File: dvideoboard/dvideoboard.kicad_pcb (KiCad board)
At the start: 2 copper layers, 64.9 x 48.1 mm, 18 parts, among them IC1 LVC245A, IC2 LVC245A, IC3 LVC245A, IC4 LVC245A, P1 CONN_02X16, P3 JTAG, U1 10M08SC, U2 ADV7513, U3 TC1262-33VDB, U4 TC1262-33VDB, U5 Si501

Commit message: Ongoing development fpga board
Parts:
- removed U4: TC1262-33VDB, TO_SOT_Packages_SMD:SOT-223
- removed U5: Si501, Oscillators:Oscillator_SMD_SeikoEpson_SG8002LB-4pin_5.0x3.2mm_HandSoldering
- added C10: 4.7uF, Capacitors_SMD:C_0805, F.Cu at (183.6, 143.6)
- added C11: 10uF, Capacitors_SMD:C_0805, B.Cu at (177.2, 129.5)
- added C12: 10uF, Capacitors_SMD:C_0805, B.Cu at (180.7, 130.4)
- added C6: 10uF, Capacitors_SMD:C_0805, F.Cu at (164.5, 137.8)
- added C7: 47u, Capacitors_SMD:C_1206, F.Cu at (185.7, 142.7)
- added C8: 4.7u, Capacitors_SMD:C_0805, F.Cu at (173.2, 143.3)
- added C9: 10uF, Capacitors_SMD:C_0805, F.Cu at (175.9, 137.8)
- added D2: LED, LEDs:LED_0805, F.Cu at (130.8, 104.1)
- added F1: 0ZCK0050AF2E, Capacitors_SMD:C_0805, F.Cu at (185.5, 138.2)
- added IC5: EP5388QI, Housings_SSOP:TSSOP-16_4.4x5mm_Pitch0.65mm, F.Cu at (167.4, 143.0)
- added IC6: EP5388QI, Housings_SSOP:TSSOP-16_4.4x5mm_Pitch0.65mm, F.Cu at (178.6, 143.0)
- added L1: 10uH, Capacitors_SMD:C_0805, F.Cu at (163.2, 134.0)
- added L2: 10uH, Capacitors_SMD:C_0805, F.Cu at (166.4, 134.0)
- added L3: 10uH, Capacitors_SMD:C_0805, F.Cu at (168.9, 134.0)
- added L4: 10uH, Capacitors_SMD:C_0805, F.Cu at (171.4, 134.0)
- added L5: 10uH, Capacitors_SMD:C_0805, F.Cu at (174.6, 134.0)
- added L6: 10uH, Capacitors_SMD:C_0805, F.Cu at (177.2, 134.0)
- added L7: 10uH, Capacitors_SMD:C_0805, F.Cu at (179.7, 134.0)
- added P2: POWER, Pin_Headers:Pin_Header_Straight_1x02_Pitch2.54mm, F.Cu at (188.8, 141.7)
- added P4: HDMI-A, footprints:FCI_10029449-11-5B13-5DRLF, F.Cu at (179.3, 119.4)
- added P5: CONN_01X02, Pin_Headers:Pin_Header_Straight_2x01_Pitch2.54mm, F.Cu at (130.8, 100.3)
- added R10: 2K, Resistors_SMD:R_0805, F.Cu at (172.7, 102.9)
- added R11: 2K, Resistors_SMD:R_0805, F.Cu at (170.2, 101.0)
- added R12: 10k, Resistors_SMD:R_0805, F.Cu at (171.4, 125.7)
- added R13: 2K, Resistors_SMD:R_0805, F.Cu at (177.8, 106.0)
- added R14: 2K, Resistors_SMD:R_0805, F.Cu at (180.3, 106.0)
- added R15: 2K, Resistors_SMD:R_0805, F.Cu at (175.3, 104.8)
- added R16: 1K, Resistors_SMD:R_0805, F.Cu at (130.8, 108.6)
- added R2: 10k, Resistors_SMD:R_0805, F.Cu at (124.5, 116.8)
- added R3: 10k, Resistors_SMD:R_0805, F.Cu at (127.0, 116.8)
- added R4: 10k, Resistors_SMD:R_0805, F.Cu at (121.9, 116.8)
- added R5: 10k, Resistors_SMD:R_0805, F.Cu at (129.5, 116.8)
- added R6: 10k, Resistors_SMD:R_0805, F.Cu at (140.3, 99.7)
- added R7: 10k, Resistors_SMD:R_0805, F.Cu at (144.1, 99.7)
- added R8: 10k, Resistors_SMD:R_0805, F.Cu at (148.6, 99.7)
- added R9: 887, Resistors_SMD:R_0805, F.Cu at (168.9, 125.7)
- C1, C2, C3, C4, C5: value 100n -> 10uF; footprint Capacitors_SMD:C_0805_HandSoldering -> Capacitors_SMD:C_0805; moved to B.Cu
- D1: value Led_Small -> LED
- IC1, IC2, IC3, IC4: value LVC245A -> SN74LVC245APWR
- R1: footprint Resistors_SMD:R_0805_HandSoldering -> Resistors_SMD:R_0805
- U1: value 10M08SC -> 10M08SCE144C8G
- U3: value TC1262-33VDB -> TG2016SBN 20.0000M-TCGNNM3; footprint TO_SOT_Packages_SMD:SOT-223 -> Crystals:Crystal_SMD_2016-4pin_2.0x1.6mm
- moved C5 51.9 mm to (174.6, 129.5), turned to 270 degrees
- moved U3 51.7 mm to (123.8, 121.9)
- moved C4 50.3 mm to (171.4, 129.5), turned to 270 degrees
- moved C3 37.6 mm to (168.9, 129.5), turned to 270 degrees
- moved C2 25.0 mm to (166.4, 129.5), turned to 270 degrees
- moved C1 11.9 mm to (163.2, 129.5), turned to 270 degrees
- moved R1 2.69 mm to (133.3, 108.6), turned to 90 degrees
- moved D1 2.01 mm to (133.3, 104.1), turned to 90 degrees
- moved U2 1.27 mm to (168.3, 116.2)
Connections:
- C1 pad 1: Net-(C1-Pad1) -> GND
- C1 pad 2: GND -> /3V3A
- C2 pad 1: Net-(C1-Pad1) -> GND
- C2 pad 2: GND -> /3V3B
- C3 pad 1: Net-(C1-Pad1) -> GND
- C3 pad 2: GND -> /3V3C
- C4 pad 1: Net-(C1-Pad1) -> GND
- C4 pad 2: GND -> /3V3D
- C5 pad 1: Net-(C1-Pad1) -> GND
- C5 pad 2: GND -> /1V8A
- D1 pad 1: GND -> Net-(D1-Pad1)
- IC1 pad 1: Net-(C1-Pad1) -> /3V3A
- IC1 pad 20: Net-(C1-Pad1) -> /3V3A
- IC2 pad 1: Net-(C1-Pad1) -> /3V3A
- IC2 pad 20: Net-(C1-Pad1) -> /3V3A
- IC3 pad 1: Net-(C1-Pad1) -> /3V3A
- IC3 pad 20: Net-(C1-Pad1) -> /3V3A
- IC4 pad 1: Net-(C1-Pad1) -> /3V3A
- IC4 pad 20: Net-(C1-Pad1) -> /3V3A
- P3 pad 4: Net-(C1-Pad1) -> /3V3A
- R1 pad 1: Net-(R1-Pad1) -> GND
- R1 pad 2: Net-(D1-Pad2) -> Net-(D1-Pad1)
- U1 pad 1: Net-(U1-Pad1) -> /3V3B
- U1 pad 103: Net-(U1-Pad103) -> /3V3B
- U1 pad 104: Net-(U1-Pad104) -> GND
- U1 pad 107: Net-(U1-Pad107) -> /3V3C
- U1 pad 108: Net-(U1-Pad108) -> /3V3B
- U1 pad 109: Net-(U1-Pad109) -> /3V3B
- U1 pad 114: Net-(U1-Pad114) -> Net-(R15-Pad2)
- U1 pad 115: Net-(U1-Pad115) -> /3V3B
- U1 pad 116: Net-(U1-Pad116) -> GND
- U1 pad 117: Net-(U1-Pad117) -> /3V3B
- U1 pad 121: Net-(U1-Pad121) -> /3V3B
- U1 pad 122: Net-(U1-Pad122) -> /3V3B
- U1 pad 125: Net-(U1-Pad125) -> GND
- U1 pad 128: Net-(U1-Pad128) -> /3V3B
- U1 pad 129: Net-(U1-Pad129) -> /3V3B
- U1 pad 133: Net-(U1-Pad133) -> GND
- U1 pad 137: Net-(U1-Pad137) -> GND
- U1 pad 139: Net-(U1-Pad139) -> /3V3B
- U1 pad 142: Net-(U1-Pad142) -> GND
- U1 pad 143: Net-(U1-Pad143) -> /3V3C
- U1 pad 144: Net-(U1-Pad144) -> /3V3B
- U1 pad 2: Net-(U1-Pad2) -> /3V3C
- U1 pad 23: Net-(U1-Pad23) -> /3V3B
- U1 pad 3: Net-(U1-Pad3) -> GND
- U1 pad 31: Net-(U1-Pad31) -> /3V3B
- U1 pad 34: Net-(U1-Pad34) -> /3V3C
- U1 pad 35: Net-(U1-Pad35) -> /3V3C
- U1 pad 36: Net-(U1-Pad36) -> /3V3B
- U1 pad 37: Net-(U1-Pad37) -> /3V3B
- U1 pad 4: Net-(U1-Pad4) -> GND
- U1 pad 40: Net-(U1-Pad40) -> /3V3B
- U1 pad 42: Net-(U1-Pad42) -> GND
- U1 pad 49: Net-(U1-Pad49) -> /3V3B
- U1 pad 5: Net-(U1-Pad5) -> /3V3C
- U1 pad 51: Net-(U1-Pad51) -> /3V3B
- U1 pad 53: Net-(U1-Pad53) -> GND
- U1 pad 6: Net-(R1-Pad1) -> Net-(D1-Pad2)
- U1 pad 63: Net-(U1-Pad63) -> GND
- U1 pad 67: Net-(U1-Pad67) -> /3V3B
- U1 pad 68: Net-(U1-Pad68) -> GND
- U1 pad 71: Net-(U1-Pad71) -> /3V3C
- U1 pad 72: Net-(U1-Pad72) -> /3V3B
- U1 pad 73: Net-(U1-Pad73) -> /3V3B
- U1 pad 82: Net-(U1-Pad82) -> /3V3B
- U1 pad 83: Net-(U1-Pad83) -> GND
- U1 pad 9: Net-(U1-Pad9) -> /3V3B
- U1 pad 94: Net-(U1-Pad94) -> /3V3B
- U1 pad 95: Net-(U1-Pad95) -> GND
- U2 pad 1: Net-(U2-Pad1) -> /1V8A
- U2 pad 10: Net-(U2-Pad10) -> GND
- U2 pad 11: Net-(U2-Pad11) -> /1V8A
- U2 pad 12: Net-(U2-Pad12) -> /1V8C
- U2 pad 13: Net-(U2-Pad13) -> /1V8C
- U2 pad 15: Net-(U2-Pad15) -> /1V8B
- U2 pad 19: Net-(U2-Pad19) -> /1V8B
- U2 pad 22: Net-(U2-Pad22) -> GND
- U2 pad 25: Net-(U2-Pad25) -> /1V8B
- U2 pad 28: Net-(U2-Pad28) -> Net-(R15-Pad2)
- U2 pad 29: Net-(U2-Pad29) -> /3V3D
- U2 pad 30: Net-(U2-Pad30) -> GND
- U2 pad 31: Net-(U2-Pad31) -> /1V8A
- U2 pad 32: Net-(U2-Pad32) -> GND
- U2 pad 4: Net-(U2-Pad4) -> GND
- U2 pad 5: Net-(U2-Pad5) -> GND
- U2 pad 51: Net-(U2-Pad51) -> /1V8A
- U2 pad 6: Net-(U2-Pad6) -> GND
- U2 pad 7: Net-(U2-Pad7) -> GND
- U2 pad 8: Net-(U2-Pad8) -> GND
- U2 pad 9: Net-(U2-Pad9) -> GND
- U3 pad 2: Net-(U3-Pad2) -> GND
- U3 pad 3: Net-(U3-Pad3) -> Net-(U1-Pad26)
- U3 pad 4: Net-(U3-Pad2) -> /3V3A
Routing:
- net /3V3B: track 0.00 -> 168.5 mm, vias 0 -> 1
- net /3V3C: track 0.00 -> 106.8 mm, vias 0 -> 12
- net /3V3A: track 0.00 -> 104.6 mm, vias 0 -> 2
- net Net-(C1-Pad1): track 93.3 -> 0.00 mm
- net /3V3D: track 0.00 -> 61.3 mm, vias 0 -> 5
- net /1V8A: track 0.00 -> 54.9 mm, vias 0 -> 1
- net GND: track 22.4 -> 75.1 mm, vias 14 -> 30
- net Net-(R15-Pad2): track 0.00 -> 41.0 mm, vias 0 -> 4
- net +5V: track 0.00 -> 39.2 mm, vias 0 -> 2
- net /1V8B: track 0.00 -> 30.9 mm, vias 0 -> 6
- net Net-(P4-Pad16): track 0.00 -> 28.9 mm
- net Net-(P4-Pad15): track 0.00 -> 27.9 mm, vias 0 -> 2
- net Net-(D2-Pad2): track 0.00 -> 21.1 mm
- net Net-(R5-Pad1): track 0.00 -> 11.7 mm, vias 0 -> 2
- net Net-(C6-Pad1): track 0.00 -> 11.1 mm
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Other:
- board size 64.9 x 48.1 mm -> 66 x 48.3 mm

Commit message: finished pcb design
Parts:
- added C13: 100nF, Capacitors_SMD:C_0805_HandSoldering, F.Cu at (151.8, 135.9)
- added C14: 100nF, Capacitors_SMD:C_0805_HandSoldering, F.Cu at (141.6, 135.9)
- added C15: 100nF, Capacitors_SMD:C_0805_HandSoldering, F.Cu at (131.4, 135.9)
- added C16: 100nF, Capacitors_SMD:C_0805_HandSoldering, F.Cu at (123.2, 126.4)
- added C17: 100nF, Capacitors_SMD:C_0805_HandSoldering, B.Cu at (153.0, 125.1)
- added C18: 100nF, Capacitors_SMD:C_0805_HandSoldering, B.Cu at (144.8, 124.5)
- added C19: 100nF, Capacitors_SMD:C_0805_HandSoldering, B.Cu at (139.1, 124.5)
- added C20: 100nF, Capacitors_SMD:C_0805_HandSoldering, B.Cu at (137.8, 117.5)
- added C21: 100nF, Capacitors_SMD:C_0805_HandSoldering, B.Cu at (137.8, 108.6)
- added C22: 100nF, Capacitors_SMD:C_0805_HandSoldering, B.Cu at (136.5, 103.5)
- added C23: 100nF, Capacitors_SMD:C_0805_HandSoldering, B.Cu at (141.6, 101.0)
- added C24: 100nF, Capacitors_SMD:C_0805_HandSoldering, B.Cu at (146.1, 101.0)
- added C25: 100nF, Capacitors_SMD:C_0805_HandSoldering, B.Cu at (149.9, 101.0)
- added C26: 100nF, Capacitors_SMD:C_0805_HandSoldering, B.Cu at (152.4, 101.0)
- added C27: 100nF, Capacitors_SMD:C_0805_HandSoldering, B.Cu at (158.8, 102.9)
- added C28: 100nF, Capacitors_SMD:C_0805_HandSoldering, B.Cu at (158.8, 108.0)
- added C29: 100nF, Capacitors_SMD:C_0805_HandSoldering, B.Cu at (158.8, 112.1)
- added C30: 100nF, Capacitors_SMD:C_0805_HandSoldering, B.Cu at (158.8, 118.1)
- added C31: 100nF, Capacitors_SMD:C_0805_HandSoldering, B.Cu at (155.6, 125.1)
- added C32: 100nF, Capacitors_SMD:C_0805_HandSoldering, B.Cu at (136.5, 120.7)
- added C33: 100nF, Capacitors_SMD:C_0805_HandSoldering, B.Cu at (140.3, 105.4)
- added C34: 100nF, Capacitors_SMD:C_0805_HandSoldering, B.Cu at (158.8, 105.4)
- added C35: 100nF, Capacitors_SMD:C_0805_HandSoldering, B.Cu at (158.1, 125.1)
- added C36: 100nF, Capacitors_SMD:C_0805_HandSoldering, B.Cu at (163.8, 123.2)
- added C37: 100nF, Capacitors_SMD:C_0805_HandSoldering, B.Cu at (161.3, 114.3)
- added C38: 100nF, Capacitors_SMD:C_0805_HandSoldering, B.Cu at (172.1, 111.1)
- added C39: 100nF, Capacitors_SMD:C_0805_HandSoldering, B.Cu at (168.3, 123.2)
- added C40: 100nF, Capacitors_SMD:C_0805_HandSoldering, B.Cu at (171.3, 120.0)
- added C41: 100nF, Capacitors_SMD:C_0805_HandSoldering, B.Cu at (173.4, 120.7)
- added C42: 100nF, Capacitors_SMD:C_0805_HandSoldering, B.Cu at (174.0, 115.6)
- added C43: 100nF, Capacitors_SMD:C_0805_HandSoldering, B.Cu at (177.8, 119.4)
- added L8: 2.2uH, Capacitors_SMD:C_0805_HandSoldering, F.Cu at (166.4, 137.2)
- added L9: 2.2uH, Capacitors_SMD:C_0805_HandSoldering, F.Cu at (175.9, 137.2)
- added R17: 450k, Resistors_SMD:R_0805_HandSoldering, F.Cu at (171.4, 138.4)
- added R18: 100k, Resistors_SMD:R_0805_HandSoldering, F.Cu at (171.4, 142.9)
- added R19: 200k, Resistors_SMD:R_0805_HandSoldering, F.Cu at (179.7, 138.4)
- added R20: 100k, Resistors_SMD:R_0805_HandSoldering, F.Cu at (179.7, 142.9)
- C1, C11, C12, C2, C3, C4, C5, F1, L1, L2, L3, L4, L5, L6, L7: footprint Capacitors_SMD:C_0805 -> Capacitors_SMD:C_0805_HandSoldering
- C10: value 4.7uF -> 4.7u; footprint Capacitors_SMD:C_0805 -> Capacitors_SMD:C_0805_HandSoldering; moved to B.Cu
- C6, C8, C9: footprint Capacitors_SMD:C_0805 -> Capacitors_SMD:C_0805_HandSoldering; moved to B.Cu
- C7: footprint Capacitors_SMD:C_1206 -> Capacitors_SMD:C_1206_HandSoldering
- IC5, IC6: value EP5388QI -> AP3417C; footprint Housings_SSOP:TSSOP-16_4.4x5mm_Pitch0.65mm -> TO_SOT_Packages_SMD:TSOT-23-5_HandSoldering
- P5: value CONN_01X02 -> CONN_01X03; footprint Pin_Headers:Pin_Header_Straight_2x01_Pitch2.54mm -> Pin_Headers:Pin_Header_Straight_1x03_Pitch2.54mm
- R1, R10, R11, R12, R13, R14, R15, R16, R2, R3, R4, R5, R6, R7, R8, R9: footprint Resistors_SMD:R_0805 -> Resistors_SMD:R_0805_HandSoldering
- U1: footprint eqfp144:QFP_144_GND -> footprints:QFP_144_GND
- moved C7 10.1 mm to (184.2, 132.7), turned to 90 degrees
- moved C10 7.25 mm to (176.5, 142.2)
- moved C8 6.31 mm to (167.0, 142.2), turned to 90 degrees
- moved P2 4.76 mm to (184.2, 141.0)
- moved C6 4.49 mm to (168.9, 137.2), turned to 270 degrees
- moved IC6 2.90 mm to (175.8, 142.2), turned to 270 degrees
- moved C9 2.62 mm to (178.4, 137.2), turned to 270 degrees
- moved R8 2.54 mm to (151.1, 99.7)
- moved F1 2.07 mm to (183.5, 137.8)
- moved R12 1.27 mm to (171.4, 127.0)
- moved R9 1.27 mm to (168.9, 127.0)
- moved IC5 1.27 mm to (166.4, 142.2), turned to 270 degrees
- moved R7 1.27 mm to (145.4, 99.7)
- moved C12 1.26 mm to (181.6, 129.5), turned to 270 degrees
- moved C1 0.64 mm to (163.8, 129.5)
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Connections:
- IC5 pad 1: Net-(IC5-Pad1) -> +5V
- IC5 pad 3: GND -> Net-(IC5-Pad3)
- IC5 pad 4: Net-(IC5-Pad4) -> +5V
- IC5 pad 5: Net-(C6-Pad1) -> Net-(IC5-Pad5)
- IC6 pad 1: Net-(IC6-Pad1) -> +5V
- IC6 pad 3: GND -> Net-(IC6-Pad3)
- IC6 pad 4: Net-(IC6-Pad4) -> +5V
- IC6 pad 5: Net-(C9-Pad1) -> Net-(IC6-Pad5)
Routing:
- net +5V: track 39.2 -> 71.8 mm, vias 2 -> 5
- net /3V3B: track 168.5 -> 197.9 mm, vias 1 -> 18
- net GND: track 75.1 -> 97.4 mm, vias 30 -> 41
- net /1V8C: track 5.48 -> 25.9 mm, vias 1 -> 4
- net /3V3A: track 104.6 -> 113.3 mm
- net Net-(D2-Pad2): track 21.1 -> 12.5 mm, vias 0 -> 2
- net Net-(P4-Pad19): track 3.69 -> 11.9 mm, vias 0 -> 2
- net /1V8A: track 54.9 -> 61.9 mm, vias 1 -> 5
- net Net-(IC5-Pad5): track 0.00 -> 6.88 mm
- net Net-(IC6-Pad5): track 0.00 -> 5.74 mm
- net Net-(C9-Pad1): track 7.96 -> 12.1 mm, vias 0 -> 1
- net Net-(C6-Pad1): track 11.1 -> 14.8 mm, vias 0 -> 1
- net Net-(IC5-Pad3): track 0.00 -> 3.49 mm
- net Net-(IC6-Pad3): track 0.00 -> 3.44 mm
- net Net-(F1-Pad2): track 0.00 -> 3.43 mm
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- added copper zone on B.Cu, net GND

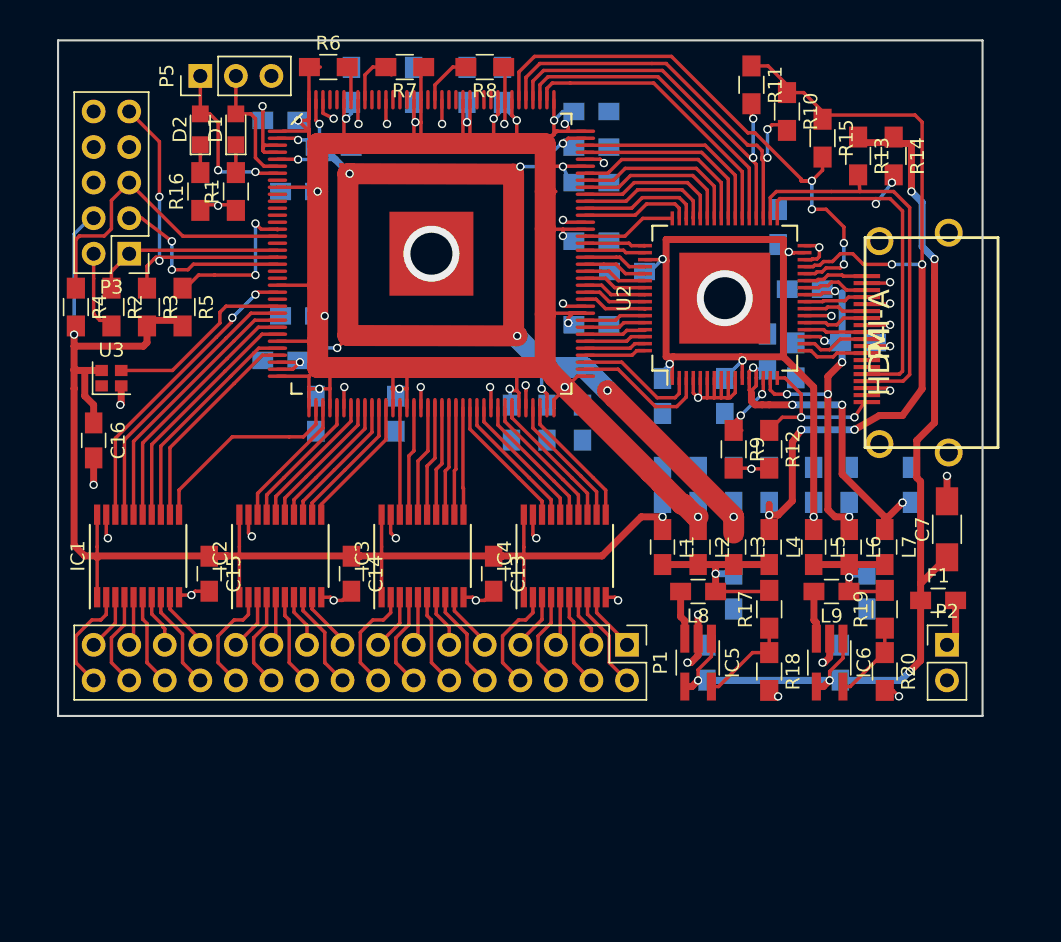
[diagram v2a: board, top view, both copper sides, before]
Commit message: first working program on the dvideo-board (lead blinker)
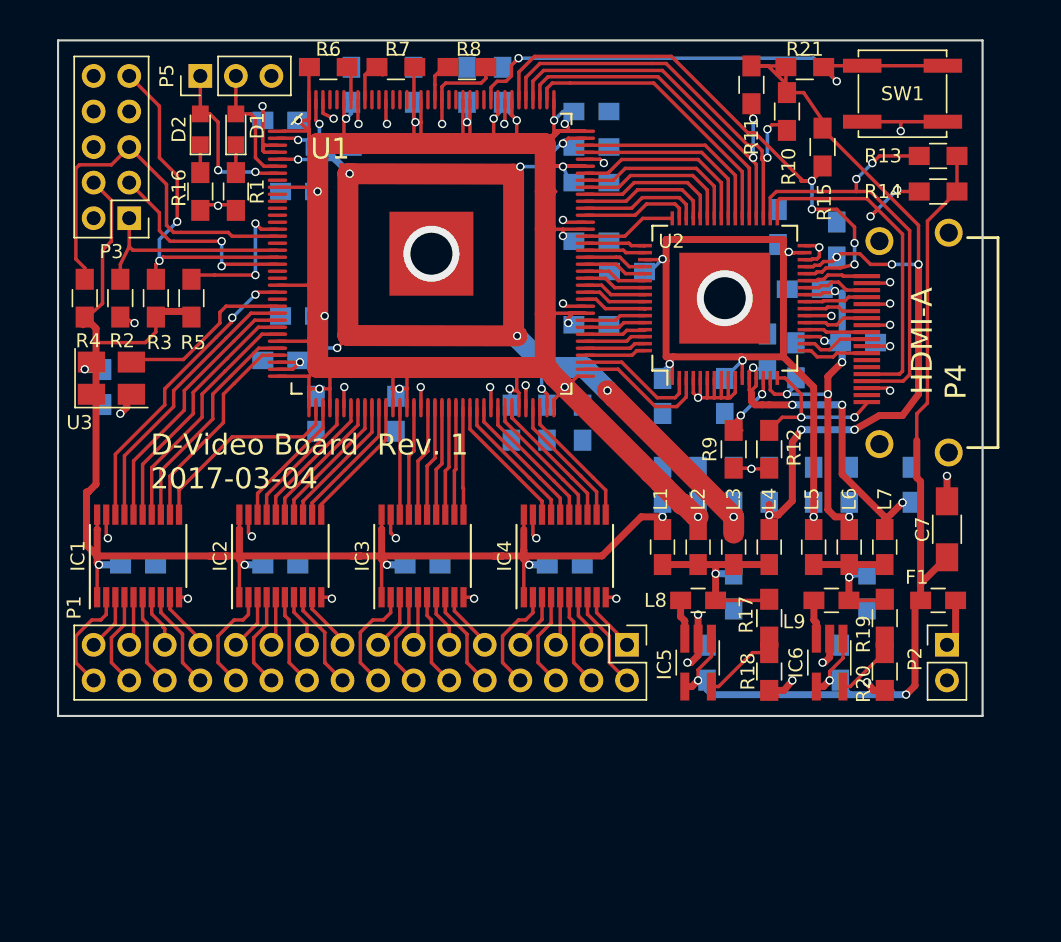
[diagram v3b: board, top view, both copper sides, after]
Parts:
- added C44: 100nF, Capacitors_SMD:C_0805_HandSoldering, B.Cu at (146.7, 135.3)
- added C45: 100nF, Capacitors_SMD:C_0805_HandSoldering, B.Cu at (176.3, 112.0)
- added R21: 10k, Resistors_SMD:R_0805_HandSoldering, F.Cu at (174.0, 99.7)
- added SW1: SKRWAEE030, Buttons_Switches_SMD:SW_SPST_EVPBF, F.Cu at (181.0, 101.6)
- C13, C14, C15, C16: moved to B.Cu
- R17: value 450k -> 450k 1%
- R18, R20: value 100k -> 100k 1%
- R19: value 200k -> 200k 1%
- R9: value 887 -> 887 1%
- U3: value TG2016SBN 20.0000M-TCGNNM3 -> LFSPXO025560; footprint Crystals:Crystal_SMD_2016-4pin_2.0x1.6mm -> Crystals:Crystal_SMD_EuroQuartz_MT-4pin_3.2x2.5mm_HandSoldering
- moved R13 5.71 mm to (183.5, 106.0), turned to 0 degrees
- moved C13 5.12 mm to (156.8, 135.3), turned to 0 degrees
- moved C15 5.12 mm to (126.4, 135.3), turned to 0 degrees
- moved C14 5.12 mm to (136.5, 135.3), turned to 0 degrees
- moved R14 4.07 mm to (183.5, 108.6), turned to 0 degrees
- moved C16 3.86 mm to (123.8, 122.6)
- moved P3 2.54 mm to (125.7, 110.5)
- moved R8 1.27 mm to (149.9, 99.7), turned to 0 degrees
- moved R5 0.90 mm to (130.2, 116.2)
- moved R2 0.90 mm to (125.1, 116.2), turned to 90 degrees
- moved R3 0.90 mm to (127.6, 116.2)
- moved R4 0.90 mm to (122.6, 116.2)
- moved L8 0.63 mm to (166.4, 137.8), turned to 0 degrees
- moved L9 0.63 mm to (175.9, 137.8), turned to 0 degrees
- moved R15 0.63 mm to (175.3, 105.4), turned to 90 degrees
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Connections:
- C1 pad 1: GND -> /3V3A
- C1 pad 2: /3V3A -> GND
- C10 pad 1: +5V -> GND
- C10 pad 2: GND -> +5V
- C11 pad 1: GND -> /1V8B
- C11 pad 2: /1V8B -> GND
- C12 pad 1: GND -> /1V8C
- C12 pad 2: /1V8C -> GND
- C2 pad 1: GND -> /3V3B
- C2 pad 2: /3V3B -> GND
- C3 pad 1: GND -> /3V3C
- C3 pad 2: /3V3C -> GND
- C4 pad 1: GND -> /3V3D
- C4 pad 2: /3V3D -> GND
- C40 pad 1: /1V8C -> GND
- C40 pad 2: GND -> /1V8C
- C5 pad 1: GND -> /1V8A
- C5 pad 2: /1V8A -> GND
- C6 pad 1: Net-(C6-Pad1) -> GND
- C6 pad 2: GND -> Net-(C6-Pad2)
- C8 pad 1: +5V -> GND
- C8 pad 2: GND -> +5V
- C9 pad 1: Net-(C9-Pad1) -> GND
- C9 pad 2: GND -> Net-(C9-Pad2)
- L1 pad 2: Net-(C6-Pad1) -> Net-(C6-Pad2)
- L2 pad 2: Net-(C6-Pad1) -> Net-(C6-Pad2)
- L3 pad 2: Net-(C6-Pad1) -> Net-(C6-Pad2)
- L4 pad 2: Net-(C6-Pad1) -> Net-(C6-Pad2)
- L5 pad 2: Net-(C9-Pad1) -> Net-(C9-Pad2)
- L6 pad 2: Net-(C9-Pad1) -> Net-(C9-Pad2)
- L7 pad 2: Net-(C9-Pad1) -> Net-(C9-Pad2)
- L8 pad 1: Net-(C6-Pad1) -> Net-(IC5-Pad3)
- L8 pad 2: Net-(IC5-Pad3) -> Net-(C6-Pad2)
- L9 pad 1: Net-(C9-Pad1) -> Net-(IC6-Pad3)
- L9 pad 2: Net-(IC6-Pad3) -> Net-(C9-Pad2)
- R1 pad 1: GND -> Net-(D1-Pad1)
- R1 pad 2: Net-(D1-Pad1) -> GND
- R10 pad 1: /3V3D -> Net-(R10-Pad1)
- R10 pad 2: Net-(R10-Pad2) -> /3V3D
- R11 pad 1: /3V3D -> Net-(R11-Pad1)
- R11 pad 2: Net-(R11-Pad2) -> /3V3D
- R12 pad 1: Net-(P4-Pad19) -> GND
- R12 pad 2: GND -> Net-(P4-Pad19)
- R13 pad 1: +5V -> Net-(P4-Pad16)
- R13 pad 2: Net-(P4-Pad16) -> +5V
- R14 pad 1: +5V -> Net-(P4-Pad15)
- R14 pad 2: Net-(P4-Pad15) -> +5V
- R15 pad 1: /3V3D -> Net-(R15-Pad1)
- R15 pad 2: Net-(R15-Pad2) -> /3V3D
- R16 pad 1: GND -> Net-(D2-Pad1)
- R16 pad 2: Net-(D2-Pad1) -> GND
- R17 pad 1: Net-(IC5-Pad5) -> Net-(C6-Pad2)
- R17 pad 2: Net-(C6-Pad1) -> Net-(IC5-Pad5)
- R18 pad 1: Net-(IC5-Pad5) -> GND
- R18 pad 2: GND -> Net-(IC5-Pad5)
- R19 pad 1: Net-(IC6-Pad5) -> Net-(C9-Pad2)
- R19 pad 2: Net-(C9-Pad1) -> Net-(IC6-Pad5)
- R2 pad 1: Net-(P3-Pad1) -> GND
- R2 pad 2: GND -> Net-(P3-Pad1)
- R20 pad 1: Net-(IC6-Pad5) -> GND
- R20 pad 2: GND -> Net-(IC6-Pad5)
- R6 pad 1: /3V3B -> Net-(R6-Pad1)
- R6 pad 2: Net-(R6-Pad2) -> /3V3B
- R7 pad 1: /3V3B -> Net-(R7-Pad1)
- R7 pad 2: Net-(R7-Pad2) -> /3V3B
- R8 pad 1: GND -> Net-(R8-Pad1)
- R8 pad 2: Net-(R8-Pad2) -> GND
- R9 pad 1: Net-(R9-Pad1) -> GND
- R9 pad 2: GND -> Net-(R9-Pad2)
- U1 pad 112: Net-(R11-Pad2) -> Net-(R11-Pad1)
- U1 pad 113: Net-(R10-Pad2) -> Net-(R10-Pad1)
- U1 pad 114: Net-(R15-Pad2) -> Net-(R15-Pad1)
- U1 pad 126: Net-(R8-Pad2) -> Net-(R8-Pad1)
- U1 pad 136: Net-(R7-Pad2) -> Net-(R7-Pad1)
- U1 pad 138: Net-(R6-Pad2) -> Net-(R6-Pad1)
- U2 pad 14: Net-(R9-Pad1) -> Net-(R9-Pad2)
- U2 pad 28: Net-(R15-Pad2) -> Net-(R15-Pad1)
- U2 pad 35: Net-(R10-Pad2) -> Net-(R10-Pad1)
- U2 pad 36: Net-(R11-Pad2) -> Net-(R11-Pad1)
- U3 pad 1: Net-(U3-Pad1) -> /3V3A
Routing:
- net Net-(R15-Pad1): track 0.00 -> 41.8 mm, vias 0 -> 4
- net Net-(R15-Pad2): track 41.0 -> 0.00 mm, vias 4 -> 0
- net Net-(R21-Pad2): track 0.00 -> 38.3 mm, vias 0 -> 2
- net GND: track 97.4 -> 132.0 mm, vias 41 -> 42
- net Net-(R10-Pad2): track 30.4 -> 0.00 mm, vias 2 -> 0
- net Net-(R10-Pad1): track 0.00 -> 30.4 mm, vias 0 -> 2
- net Net-(R11-Pad2): track 28.8 -> 0.00 mm, vias 2 -> 0
- net Net-(R11-Pad1): track 0.00 -> 28.8 mm, vias 0 -> 2
- net Net-(C6-Pad2): track 0.00 -> 15.4 mm, vias 0 -> 1
- net /3V3A: track 113.3 -> 128.6 mm, vias 2 -> 6
- net Net-(C6-Pad1): track 14.8 -> 0.00 mm, vias 1 -> 0
- net /3V3B: track 197.9 -> 211.6 mm
- net Net-(C9-Pad2): track 0.00 -> 12.7 mm, vias 0 -> 1
- net Net-(C9-Pad1): track 12.1 -> 0.00 mm, vias 1 -> 0
- net Net-(R9-Pad2): track 0.00 -> 5.21 mm, vias 0 -> 2
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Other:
- board text added: "D-Video Board Rev. 1 2017-03-04"
- board text added: "U1"
